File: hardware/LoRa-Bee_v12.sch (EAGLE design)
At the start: 19 parts, among them IC1 RFM9XW, J1 JUMPER3-0603, X1 PASSER-07, X2 PASSER-07, X3 PASSER-07

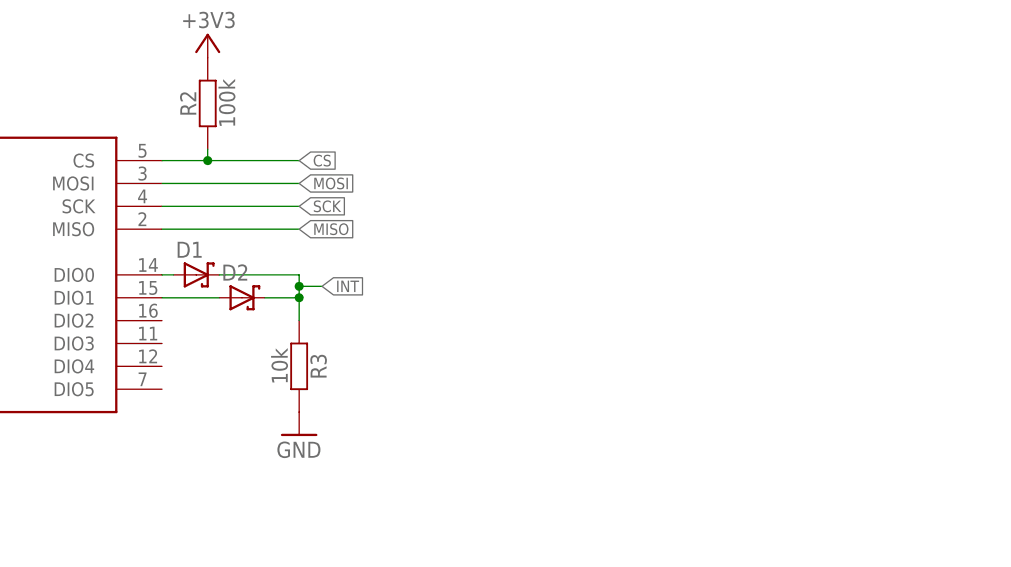
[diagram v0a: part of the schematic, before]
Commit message: updated schematics
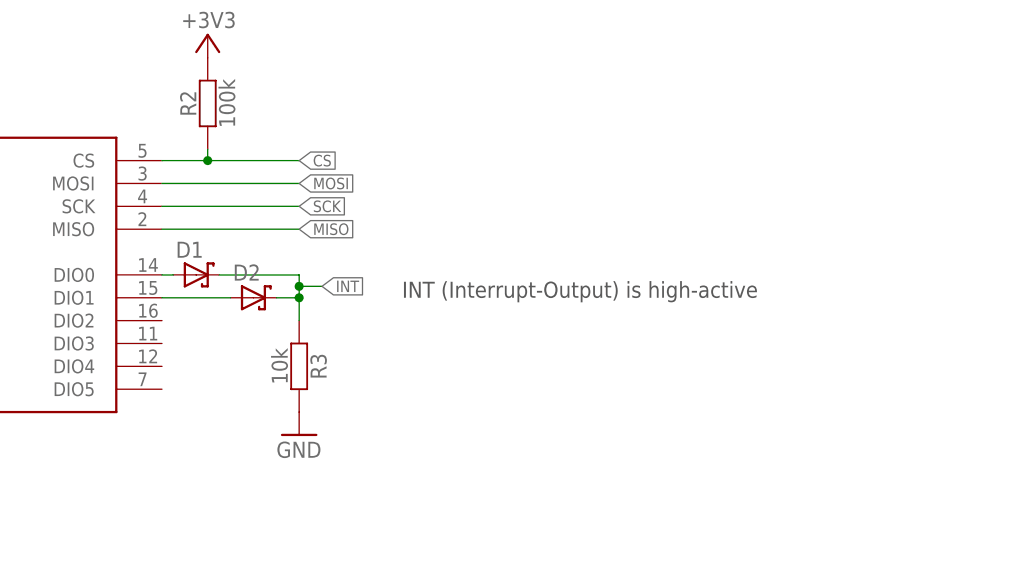
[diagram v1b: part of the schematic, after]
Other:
- note added: "INT (Interrupt-Output) is high-active"
- moved on the sheet: D2
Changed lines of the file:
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@@
 <setting verticaltext="up"/>
 </settings>
-<grid distance="0.1" unitdist="inch" unit="inch" style="lines" multiple="1" display="no" altdistance="0.01" altunitdist="inch" altunit="inch"/>
+<grid distance="0.05" unitdist="inch" unit="inch" style="lines" multiple="1" display="yes" altdistance="0.01" altunitdist="inch" altunit="inch"/>
 <layers>
 <layer number="1" name="Top" color="4" fill="1" visible="no" active="no"/>
@@
 License. http://creativecommons.org/licenses/by-sa/4.0/
 Designed by Watterott electronic</text>
+<text x="162.56" y="107.95" size="1.778" layer="97">INT (Interrupt-Output) is high-active</text>
 </plain>
 <instances>
@@
 <instance part="R3" gate="R" x="151.13" y="100.33" rot="R270"/>
 <instance part="D1" gate="D" x="139.7" y="110.49"/>
-<instance part="D2" gate="D" x="144.78" y="107.95"/>
+<instance part="D2" gate="D" x="146.05" y="107.95"/>
 <instance part="GND1" gate="1" x="151.13" y="92.71" smashed="yes">
 <attribute name="VALUE" x="148.59" y="90.17" size="1.778" layer="96"/>
@@
 <wire x1="142.24" y1="110.49" x2="151.13" y2="110.49" width="0.1524" layer="91"/>
 <pinref part="D2" gate="D" pin="C"/>
-<wire x1="147.32" y1="107.95" x2="151.13" y2="107.95" width="0.1524" layer="91"/>
+<wire x1="148.59" y1="107.95" x2="151.13" y2="107.95" width="0.1524" layer="91"/>
 <junction x="151.13" y="107.95"/>
 </segment>
@@
 <pinref part="IC1" gate="IC" pin="DIO1"/>
 <pinref part="D2" gate="D" pin="A"/>
-<wire x1="135.89" y1="107.95" x2="142.24" y2="107.95" width="0.1524" layer="91"/>
-</segment>
-</net>
+<wire x1="135.89" y1="107.95" x2="143.51" y2="107.95" width="0.1524" layer="91"/>
+</segment>
+</net>
